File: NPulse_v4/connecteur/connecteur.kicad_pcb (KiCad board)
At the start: 4 copper layers, 39.8 x 44 mm, 71 parts, among them J10 Conn_02x05_Odd_Even, J13 Conn_02x05_Odd_Even, J32 Conn_02x05_Odd_Even, J35 Conn_02x05_Odd_Even, J54 Conn_02x05_Odd_Even, J57 Conn_02x05_Odd_Even, M1_1 Conn_01x01, M1_2 Conn_01x01, M2_1 Conn_01x01, M2_2 Conn_01x01, M3_1 Conn_01x01, M3_2 Conn_01x01, M4_1 Conn_01x01, M4_2 Conn_01x01, M5_1 Conn_01x01, M5_2 Conn_01x01, M6_1 Conn_01x01, M6_2 Conn_01x01, M7_1 Conn_01x01, M7_2 Conn_01x01, M8_1 Conn_01x01, M8_2 Conn_01x01

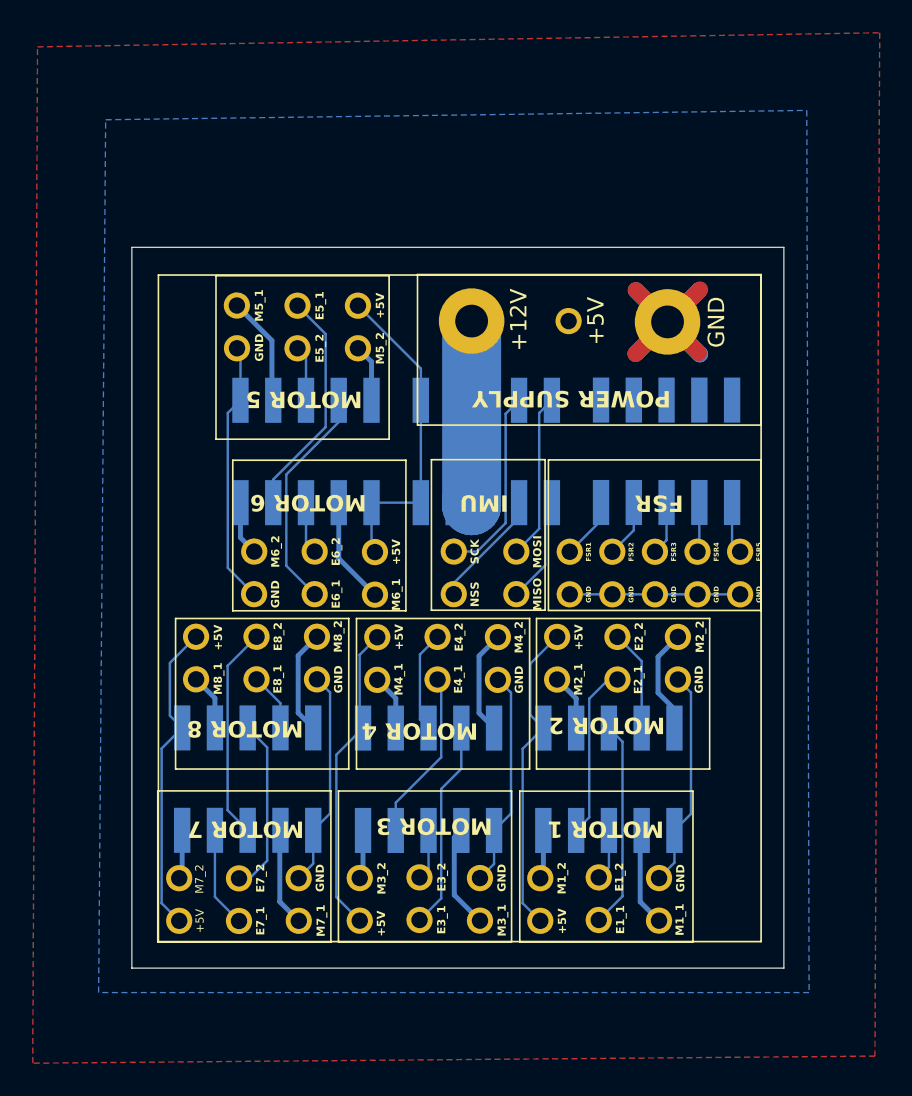
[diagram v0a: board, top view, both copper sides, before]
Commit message: Udate mounting holes positions
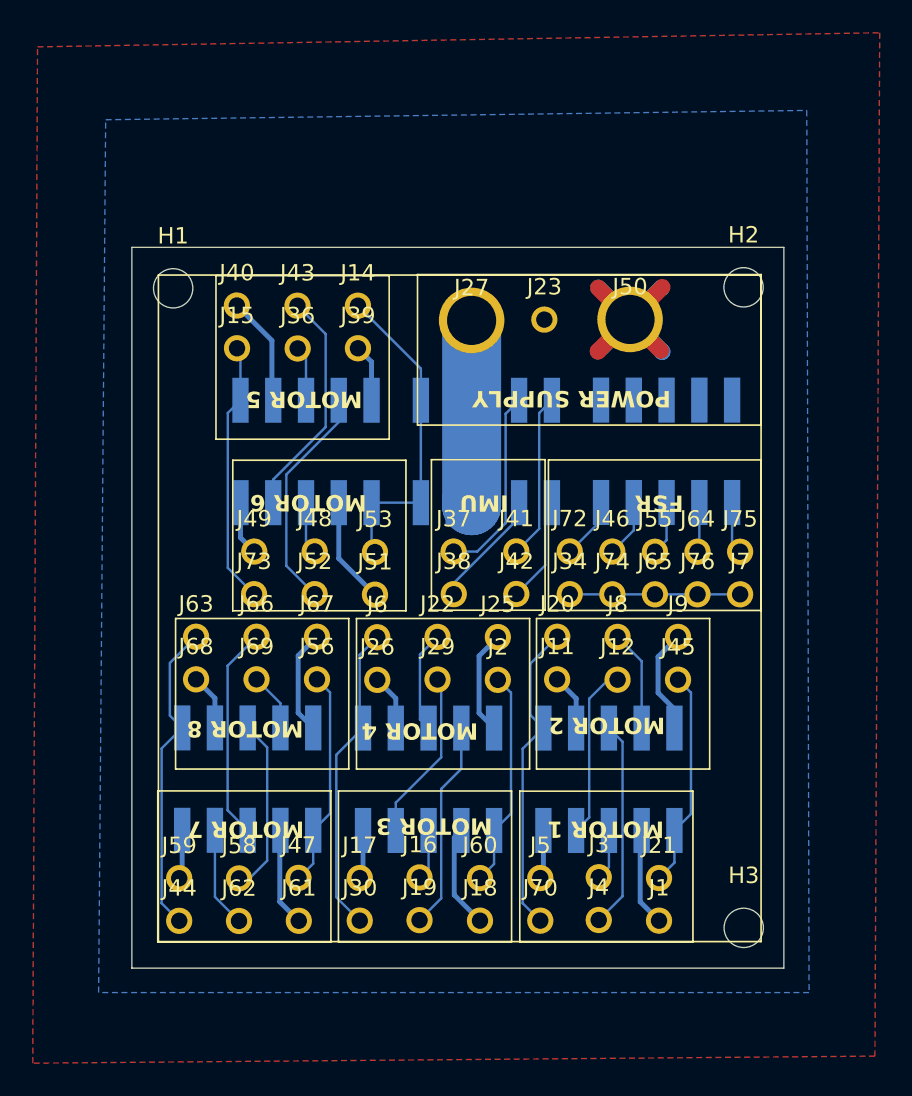
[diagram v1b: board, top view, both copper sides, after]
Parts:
- removed +12V, +5V (x9), E1_1, E1_2, E2_1, E2_2, E3_1, E3_2, E4_1, E4_2, E5_1, E5_2, E6_1, E6_2, E7_1, E7_2, E8_1, E8_2, FSR1, FSR2, FSR3, FSR4, FSR5, GND (x14), M1_1, M1_2, M2_1, M2_2, M3_1, M3_2, M4_1, M4_2, M5_1, M5_2, M6_1, M6_2, M7_1, M7_2, M8_1, M8_2, MISO, MOSI, NSS, SCK: Conn_01x01, Connector_Wire:SolderWire-0.1sqmm_1x01_D0.4mm_OD1mm
- added H1: MountingHole, MountingHole:MountingHole_2.2mm_M2, F.Cu at (149.8, 82.3)
- added H2: MountingHole, MountingHole:MountingHole_2.2mm_M2, F.Cu at (184.6, 82.3)
- added H3: MountingHole, MountingHole:MountingHole_2.2mm_M2, F.Cu at (184.7, 121.4)
- added J1: Conn_01x01, Connector_Wire:SolderWire-0.1sqmm_1x01_D0.4mm_OD1mm, F.Cu at (179.5, 120.9)
- added J11: Conn_01x01, Connector_Wire:SolderWire-0.1sqmm_1x01_D0.4mm_OD1mm, F.Cu at (173.3, 106.2)
- added J12: Conn_01x01, Connector_Wire:SolderWire-0.1sqmm_1x01_D0.4mm_OD1mm, F.Cu at (176.9, 106.2)
- added J14: Conn_01x01, Connector_Wire:SolderWire-0.1sqmm_1x01_D0.4mm_OD1mm, F.Cu at (161.1, 83.4)
- added J15: Conn_01x01, Connector_Wire:SolderWire-0.1sqmm_1x01_D0.4mm_OD1mm, F.Cu at (153.7, 86.0)
- added J16: Conn_01x01, Connector_Wire:SolderWire-0.1sqmm_1x01_D0.4mm_OD1mm, F.Cu at (164.9, 118.3)
- added J17: Conn_01x01, Connector_Wire:SolderWire-0.1sqmm_1x01_D0.4mm_OD1mm, F.Cu at (161.2, 118.3)
- added J18: Conn_01x01, Connector_Wire:SolderWire-0.1sqmm_1x01_D0.4mm_OD1mm, F.Cu at (168.6, 120.9)
- added J19: Conn_01x01, Connector_Wire:SolderWire-0.1sqmm_1x01_D0.4mm_OD1mm, F.Cu at (164.9, 120.9)
- added J2: Conn_01x01, Connector_Wire:SolderWire-0.1sqmm_1x01_D0.4mm_OD1mm, F.Cu at (169.6, 106.2)
- added J20: Conn_01x01, Connector_Wire:SolderWire-0.1sqmm_1x01_D0.4mm_OD1mm, F.Cu at (173.3, 103.6)
- added J21: Conn_01x01, Connector_Wire:SolderWire-0.1sqmm_1x01_D0.4mm_OD1mm, F.Cu at (179.5, 118.3)
- added J22: Conn_01x01, Connector_Wire:SolderWire-0.1sqmm_1x01_D0.4mm_OD1mm, F.Cu at (166.0, 103.6)
- added J23: Conn_01x01, Connector_Wire:SolderWire-0.1sqmm_1x01_D0.4mm_OD1mm, F.Cu at (172.5, 84.2)
- added J25: Conn_01x01, Connector_Wire:SolderWire-0.1sqmm_1x01_D0.4mm_OD1mm, F.Cu at (169.6, 103.6)
- added J26: Conn_01x01, Connector_Wire:SolderWire-0.1sqmm_1x01_D0.4mm_OD1mm, F.Cu at (162.3, 106.2)
- added J27: Conn_01x01, Connector_Wire:SolderWire-0.1sqmm_1x01_D0.4mm_OD1mm, F.Cu at (168.0, 84.3)
- added J29: Conn_01x01, Connector_Wire:SolderWire-0.1sqmm_1x01_D0.4mm_OD1mm, F.Cu at (166.0, 106.2)
- added J3: Conn_01x01, Connector_Wire:SolderWire-0.1sqmm_1x01_D0.4mm_OD1mm, F.Cu at (175.8, 118.3)
- added J30: Conn_01x01, Connector_Wire:SolderWire-0.1sqmm_1x01_D0.4mm_OD1mm, F.Cu at (161.2, 120.9)
- added J34: Conn_01x01, Connector_Wire:SolderWire-0.1sqmm_1x01_D0.4mm_OD1mm, F.Cu at (174.0, 101.0)
- added J36: Conn_01x01, Connector_Wire:SolderWire-0.1sqmm_1x01_D0.4mm_OD1mm, F.Cu at (157.4, 86.0)
- added J37: Conn_01x01, Connector_Wire:SolderWire-0.1sqmm_1x01_D0.4mm_OD1mm, F.Cu at (166.9, 98.4)
- added J38: Conn_01x01, Connector_Wire:SolderWire-0.1sqmm_1x01_D0.4mm_OD1mm, F.Cu at (166.9, 101.0)
- added J39: Conn_01x01, Connector_Wire:SolderWire-0.1sqmm_1x01_D0.4mm_OD1mm, F.Cu at (161.1, 86.0)
- added J4: Conn_01x01, Connector_Wire:SolderWire-0.1sqmm_1x01_D0.4mm_OD1mm, F.Cu at (175.8, 120.9)
- added J40: Conn_01x01, Connector_Wire:SolderWire-0.1sqmm_1x01_D0.4mm_OD1mm, F.Cu at (153.7, 83.4)
- added J41: Conn_01x01, Connector_Wire:SolderWire-0.1sqmm_1x01_D0.4mm_OD1mm, F.Cu at (170.8, 98.4)
- added J42: Conn_01x01, Connector_Wire:SolderWire-0.1sqmm_1x01_D0.4mm_OD1mm, F.Cu at (170.8, 101.0)
- added J43: Conn_01x01, Connector_Wire:SolderWire-0.1sqmm_1x01_D0.4mm_OD1mm, F.Cu at (157.4, 83.4)
- added J44: Conn_01x01, Connector_Wire:SolderWire-0.1sqmm_1x01_D0.4mm_OD1mm, F.Cu at (150.2, 121.0)
- added J45: Conn_01x01, Connector_Wire:SolderWire-0.1sqmm_1x01_D0.4mm_OD1mm, F.Cu at (180.6, 106.2)
- added J46: Conn_01x01, Connector_Wire:SolderWire-0.1sqmm_1x01_D0.4mm_OD1mm, F.Cu at (176.6, 98.4)
- added J47: Conn_01x01, Connector_Wire:SolderWire-0.1sqmm_1x01_D0.4mm_OD1mm, F.Cu at (157.5, 118.3)
- added J48: Conn_01x01, Connector_Wire:SolderWire-0.1sqmm_1x01_D0.4mm_OD1mm, F.Cu at (158.5, 98.4)
- added J49: Conn_01x01, Connector_Wire:SolderWire-0.1sqmm_1x01_D0.4mm_OD1mm, F.Cu at (154.8, 98.4)
- added J5: Conn_01x01, Connector_Wire:SolderWire-0.1sqmm_1x01_D0.4mm_OD1mm, F.Cu at (172.2, 118.3)
- added J50: Conn_01x01, Connector_Wire:SolderWire-0.1sqmm_1x01_D0.4mm_OD1mm, F.Cu at (177.7, 84.2)
- added J51: Conn_01x01, Connector_Wire:SolderWire-0.1sqmm_1x01_D0.4mm_OD1mm, F.Cu at (162.1, 101.0)
- added J52: Conn_01x01, Connector_Wire:SolderWire-0.1sqmm_1x01_D0.4mm_OD1mm, F.Cu at (158.5, 101.0)
- added J53: Conn_01x01, Connector_Wire:SolderWire-0.1sqmm_1x01_D0.4mm_OD1mm, F.Cu at (162.1, 98.4)
- added J55: Conn_01x01, Connector_Wire:SolderWire-0.1sqmm_1x01_D0.4mm_OD1mm, F.Cu at (179.2, 98.4)
- added J56: Conn_01x01, Connector_Wire:SolderWire-0.1sqmm_1x01_D0.4mm_OD1mm, F.Cu at (158.6, 106.2)
- added J58: Conn_01x01, Connector_Wire:SolderWire-0.1sqmm_1x01_D0.4mm_OD1mm, F.Cu at (153.8, 118.4)
- added J59: Conn_01x01, Connector_Wire:SolderWire-0.1sqmm_1x01_D0.4mm_OD1mm, F.Cu at (150.2, 118.3)
- added J6: Conn_01x01, Connector_Wire:SolderWire-0.1sqmm_1x01_D0.4mm_OD1mm, F.Cu at (162.3, 103.6)
- added J60: Conn_01x01, Connector_Wire:SolderWire-0.1sqmm_1x01_D0.4mm_OD1mm, F.Cu at (168.6, 118.3)
- added J61: Conn_01x01, Connector_Wire:SolderWire-0.1sqmm_1x01_D0.4mm_OD1mm, F.Cu at (157.5, 121.0)
- added J62: Conn_01x01, Connector_Wire:SolderWire-0.1sqmm_1x01_D0.4mm_OD1mm, F.Cu at (153.8, 121.0)
- added J63: Conn_01x01, Connector_Wire:SolderWire-0.1sqmm_1x01_D0.4mm_OD1mm, F.Cu at (151.2, 103.6)
- added J64: Conn_01x01, Connector_Wire:SolderWire-0.1sqmm_1x01_D0.4mm_OD1mm, F.Cu at (181.8, 98.4)
- added J65: Conn_01x01, Connector_Wire:SolderWire-0.1sqmm_1x01_D0.4mm_OD1mm, F.Cu at (179.2, 101.0)
- added J66: Conn_01x01, Connector_Wire:SolderWire-0.1sqmm_1x01_D0.4mm_OD1mm, F.Cu at (154.9, 103.6)
- added J67: Conn_01x01, Connector_Wire:SolderWire-0.1sqmm_1x01_D0.4mm_OD1mm, F.Cu at (158.6, 103.6)
- added J68: Conn_01x01, Connector_Wire:SolderWire-0.1sqmm_1x01_D0.4mm_OD1mm, F.Cu at (151.2, 106.2)
- added J69: Conn_01x01, Connector_Wire:SolderWire-0.1sqmm_1x01_D0.4mm_OD1mm, F.Cu at (154.9, 106.2)
- added J7: Conn_01x01, Connector_Wire:SolderWire-0.1sqmm_1x01_D0.4mm_OD1mm, F.Cu at (184.4, 101.0)
- added J70: Conn_01x01, Connector_Wire:SolderWire-0.1sqmm_1x01_D0.4mm_OD1mm, F.Cu at (172.2, 120.9)
- added J72: Conn_01x01, Connector_Wire:SolderWire-0.1sqmm_1x01_D0.4mm_OD1mm, F.Cu at (174.0, 98.4)
- added J73: Conn_01x01, Connector_Wire:SolderWire-0.1sqmm_1x01_D0.4mm_OD1mm, F.Cu at (154.8, 101.0)
- added J74: Conn_01x01, Connector_Wire:SolderWire-0.1sqmm_1x01_D0.4mm_OD1mm, F.Cu at (176.6, 101.0)
- added J75: Conn_01x01, Connector_Wire:SolderWire-0.1sqmm_1x01_D0.4mm_OD1mm, F.Cu at (184.4, 98.4)
- added J76: Conn_01x01, Connector_Wire:SolderWire-0.1sqmm_1x01_D0.4mm_OD1mm, F.Cu at (181.8, 101.0)
- added J8: Conn_01x01, Connector_Wire:SolderWire-0.1sqmm_1x01_D0.4mm_OD1mm, F.Cu at (176.9, 103.6)
- added J9: Conn_01x01, Connector_Wire:SolderWire-0.1sqmm_1x01_D0.4mm_OD1mm, F.Cu at (180.6, 103.6)

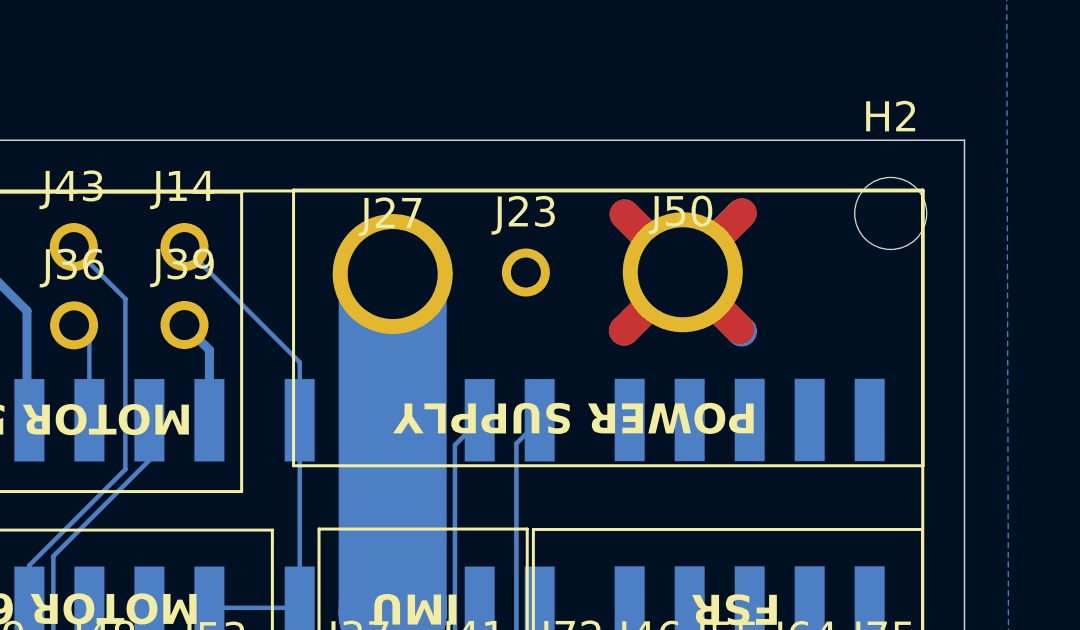
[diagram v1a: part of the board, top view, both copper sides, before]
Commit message: add 5v-gnd pair
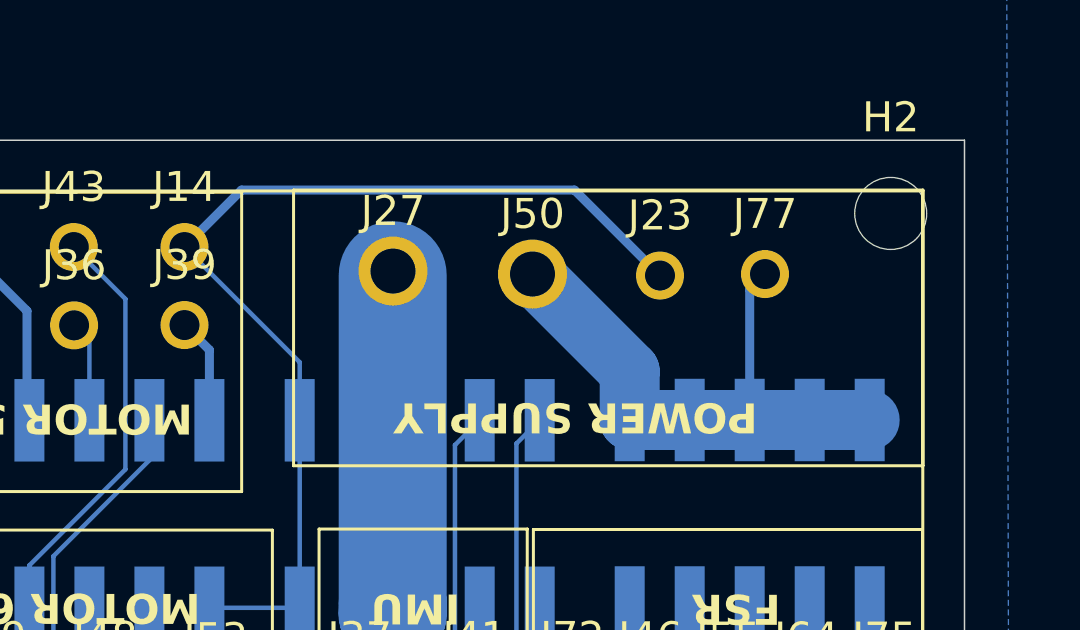
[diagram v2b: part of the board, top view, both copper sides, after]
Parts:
- added J77: Conn_01x01, Connector_Wire:SolderWire-0.1sqmm_1x01_D0.4mm_OD1mm, F.Cu at (180.4, 84.3)
- moved J50 5.01 mm to (172.7, 84.3)
- moved J23 4.47 mm to (176.9, 84.3)
- moved J27 0.10 mm to (168.1, 84.2)
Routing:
- net +5V: track 77.4 -> 95.2 mm
- net GND: track 87.9 -> 101.3 mm
- net /+12V: track 22.5 -> 11.5 mm
- added copper zone on In1.Cu, net GND
- removed copper zone on In1.Cu, net /+12V

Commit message: generate gerber files
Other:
- board text added: "12V"
- board text added: "5V"
- board text added: "E1_1"
- board text added: "E1_2"
- board text added: "E2_1"
- board text added: "E2_2"
- board text added: "E3_1"
- board text added: "E3_2"
- board text added: "E4_1"
- board text added: "E4_2"
- board text added: "E5_1"
- board text added: "E5_2"
- board text added: "E6_1"
- board text added: "E6_2"
- board text added: "E7_1"
- board text added: "E7_2"
- board text added: "E8_1"
- board text added: "E8_2"
- board text added: "FSR1"
- board text added: "FSR2"
- board text added: "FSR3"
- board text added: "FSR4"
- board text added: "FSR5"
- board text added: "GND"
- board text added: "M1_1"
- board text added: "M1_2"
- board text added: "M2_1"
- board text added: "M2_2"
- board text added: "M3_1"
- board text added: "M3_2"
- board text added: "M4_1"
- board text added: "M4_2"
- board text added: "M5_1"
- board text added: "M5_2"
- board text added: "M6_1"
- board text added: "M6_2"
- board text added: "M7_1"
- board text added: "M7_2"
- board text added: "M8_1"
- board text added: "M8_2"
- board text added: "MISO"
- board text added: "MOSI"
- board text added: "NSS"
- board text added: "SCK"
